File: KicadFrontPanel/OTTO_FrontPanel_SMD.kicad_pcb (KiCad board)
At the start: 2 copper layers, 294.5 x 102.3 mm, 75 parts, among them SW1 ALPS SKHC, SW10 ALPS SKHC, SW11 ALPS SKHC, SW12 ALPS SKHC, SW13 ALPS SKHC, SW14 ALPS SKHC, SW15 ALPS SKHC, SW16 ALPS SKHC, SW17 ALPS SKHC, SW18 ALPS SKHC, SW19 ALPS SKHC, SW2 ALPS SKHC, SW20 ALPS SKHC, SW21 ALPS SKHC, SW22 ALPS SKHC, SW23 ALPS SKHC, SW24 ALPS SKHC, SW25 ALPS SKHC, SW26 ALPS SKHC, SW3 ALPS SKHC, SW32 6x6x13mm, SW33 6x6x13mm, SW38 6x6x13mm, SW4 ALPS SKHC, SW5 ALPS SKHC, SW6 ALPS SKHC, SW7 ALPS SKHC, SW8 ALPS SKHC, SW9 ALPS SKHC

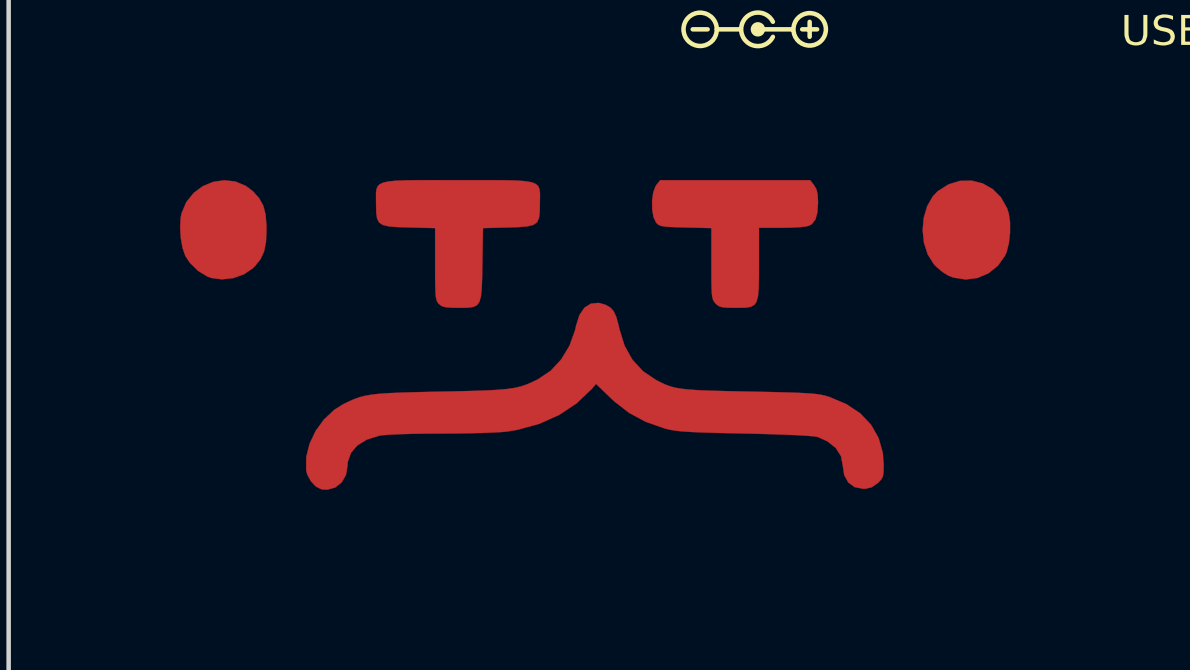
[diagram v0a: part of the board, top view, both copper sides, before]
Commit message: Changed relief logo
Now the relief logo is actually a relief
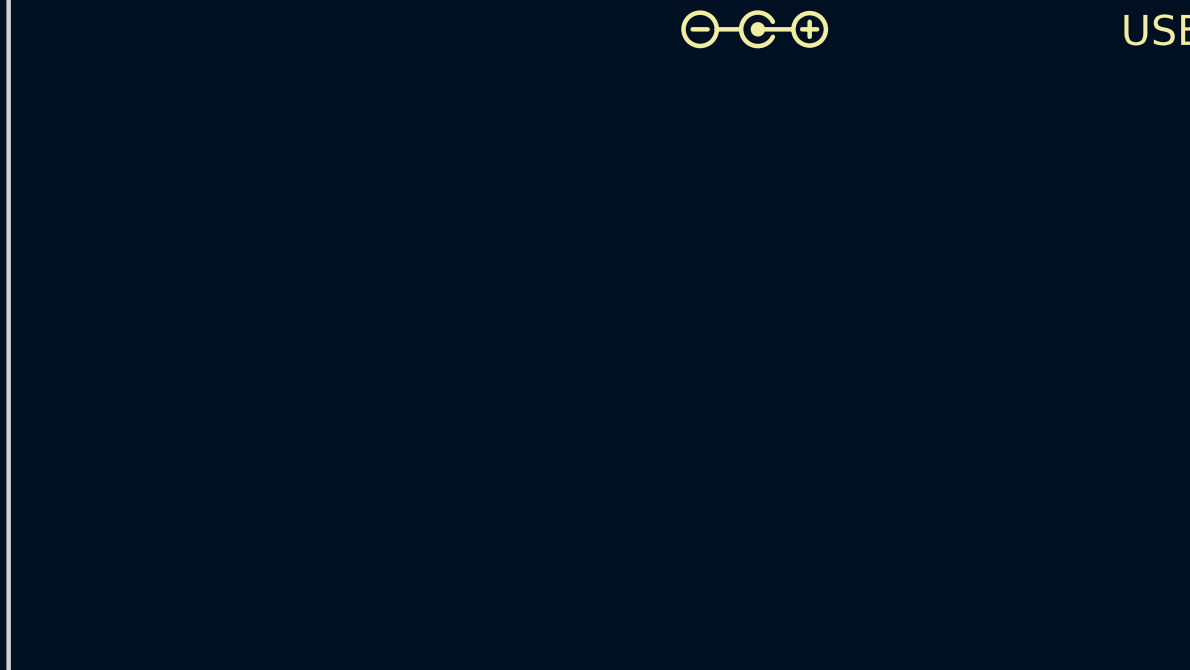
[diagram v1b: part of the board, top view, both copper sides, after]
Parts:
- removed the G*** at (33.5, 20.7)

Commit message: Added version to silkscreen on frontplates
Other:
- board text added: "v0.2.0 - SILK"
